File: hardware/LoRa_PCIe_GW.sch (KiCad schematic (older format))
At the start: 47 parts, among them U100 SX1303

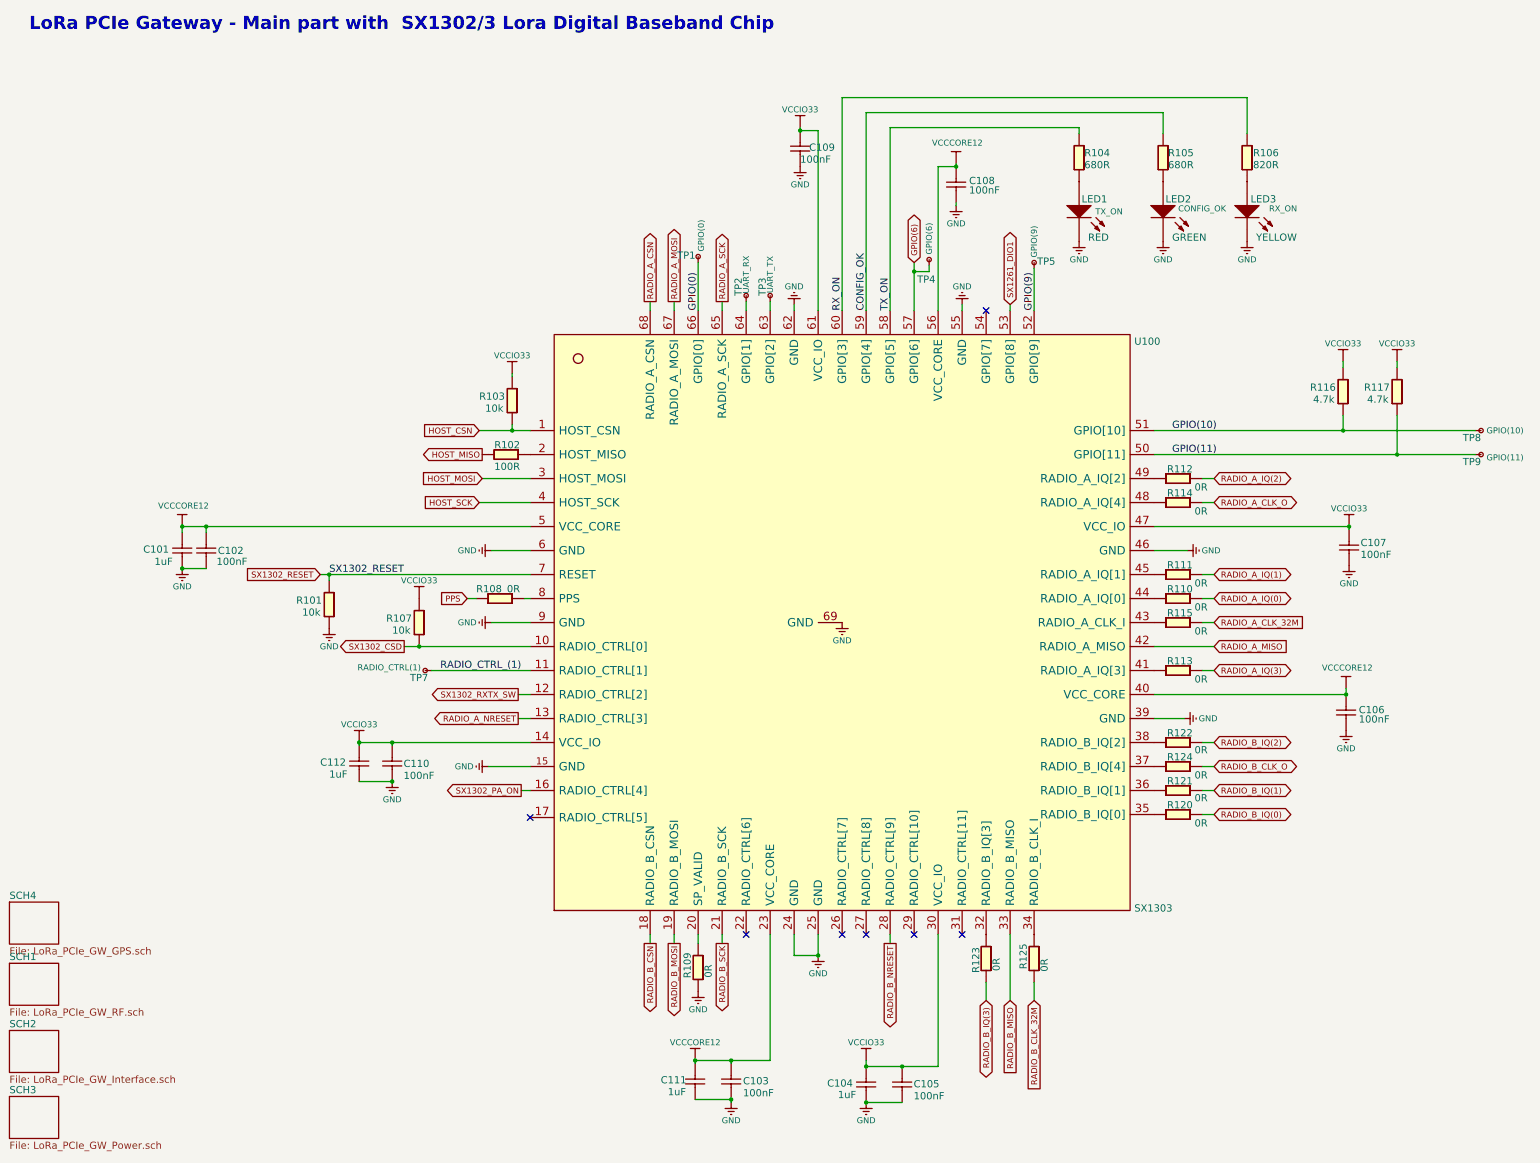
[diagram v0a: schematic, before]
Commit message: Updates according to Corecell_V3 Reference design.
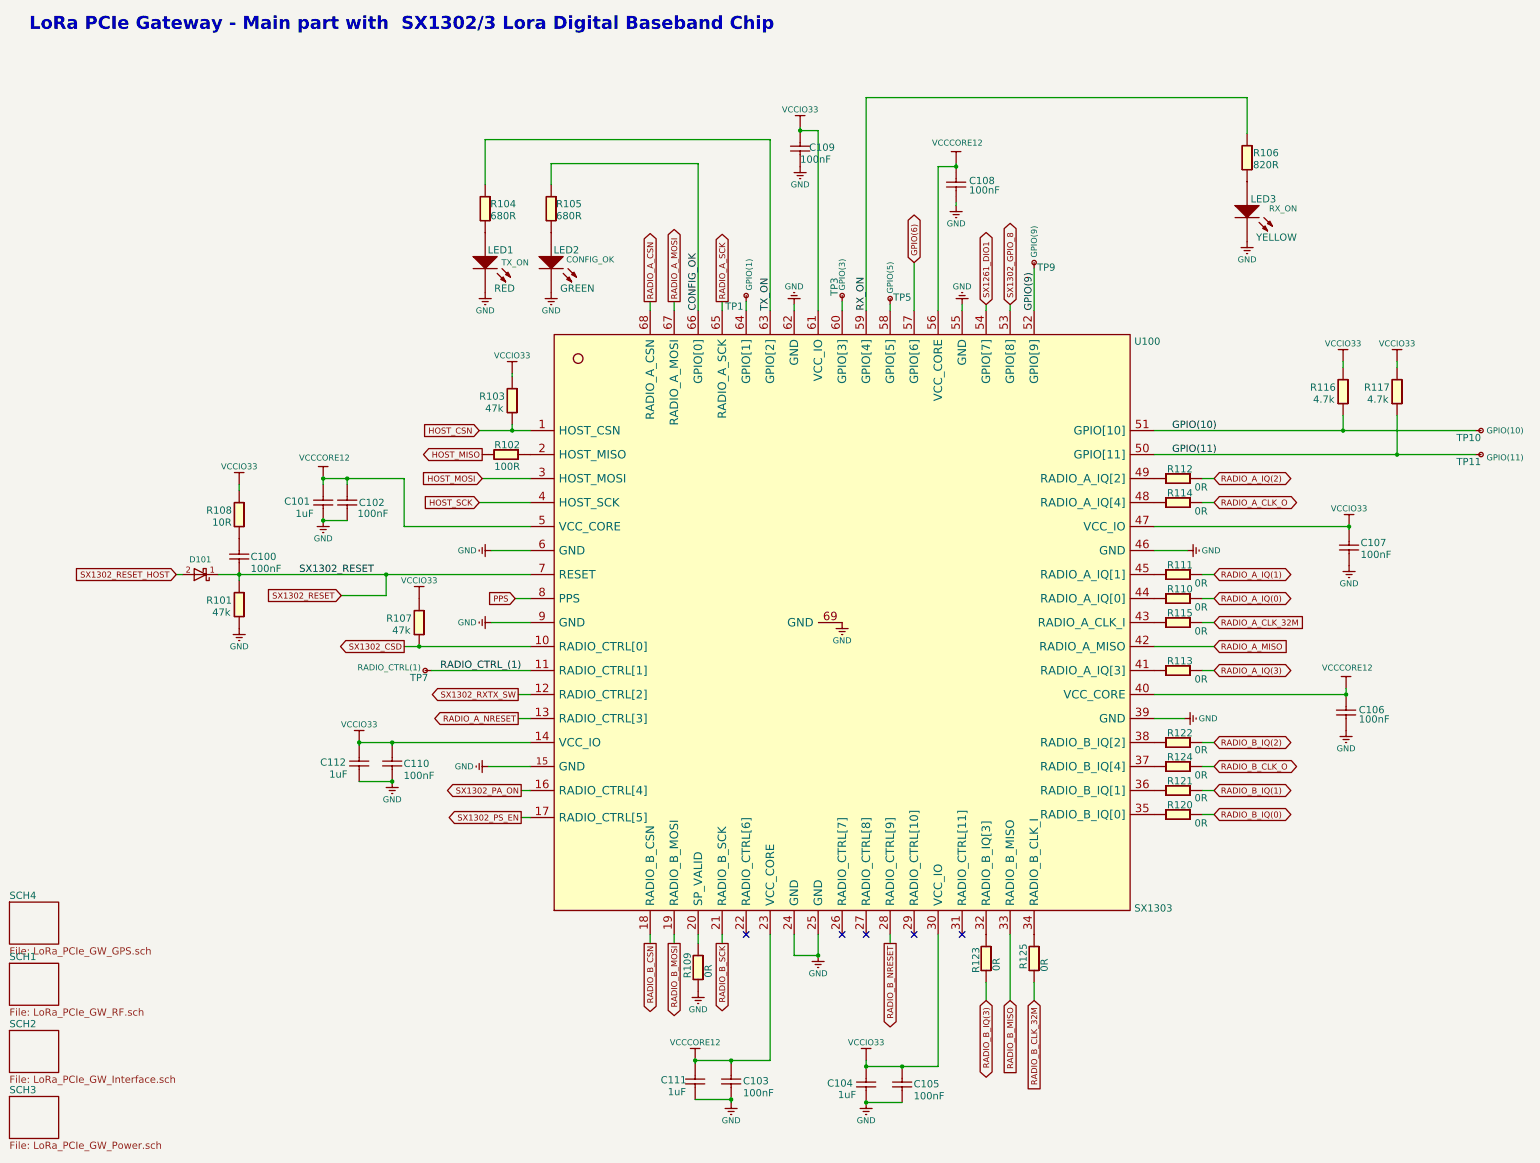
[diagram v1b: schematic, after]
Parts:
- removed TP2: NC, LoRa_PCIe_GW:PIN_SMD, symbol LoRa_PCIe_GW-rescue:test_pin-
- added C100: 100nF, LoRa_PCIe_GW:ccer_201_smd_small, symbol LoRa_PCIe_GW-rescue:Cap-
- added D101: BAT54, LoRa_PCIe_GW:SOD523, symbol LoRa_PCIe_GW-rescue:D_Schottky
- R101, R103, R107: value 10k -> 47k; Description 10 kOhms ±1% 0.05W, 1/20W Chip Resistor 0201 Thick Film -> 47 kOhms ±5% 0.05W, 1/20W Chip Resistor 0201 Thick Film; Part Number CRCW020110K0 -> CRCW020147K0; Price[1k] 0.037 -> 0.039; Supplier Link https://www.digikey.com/en/products/detail/vishay-dale/CRCW020110K0FKED/1967989 -> https://www.digikey.com/en/products/detail/vishay-dale/CRCW020147K0FKED/1968131
- R108: value 0R -> 10R; Description 0 Ohms Jumper 0.05W, 1/20W Chip Resistor 0201 (0603 Metric)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 -> 10 Ohms ±5% 0.05W, 1/20W Chip Resistor 0201 Thick Film; Part Number CRCW02010000Z0ED -> CRCW020110R0JNED; Price[1k] 0.006 -> 0.0052; Supplier Link https://www.digikey.com/en/products/detail/vishay-dale/CRCW02010000Z0ED/1178434?s=N4IgTCBcDaIMICU4HUAMZUEZU9QLVQFEAREAXQF8g -> https://www.digikey.com/en/products/detail/vishay-dale/CRCW020147K0FKED/1968131
- TP1: Label GPIO(0) -> GPIO(1)
- TP3: Label UART_TX -> GPIO(3)
- TP5: Label GPIO(9) -> GPIO(5)
- TP9: renamed from TP4; Label GPIO(6) -> GPIO(9)
- renumbered TP8 to TP10, TP9 to TP11
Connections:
- net CONFIG_OK: now also U100.66 (GPIO[0]); no longer U100.59 (GPIO[4])
- net GPIO(6): no longer TP9.1 (pin)
- net GPIO(9): now also TP9.1 (pin); no longer TP5.1 (pin)
- net PPS: now also U100.8 (PPS); no longer R108.1
- net RX_ON: now also U100.59 (GPIO[4]); no longer U100.60 (GPIO[3])
- net SX1261_DIO1: now also U100.54 (GPIO[7]); no longer U100.53 (GPIO[8])
- net SX1302_RESET: now also C100.1, D101.1
- net TX_ON: now also U100.63 (GPIO[2]); no longer U100.58 (GPIO[5])
- net VCCIO33: now also R108.2
- net SX1302_PS_EN: now reaches U100.17 (RADIO_CTRL[5])
- net at TP3.1 (pin): now also U100.60 (GPIO[3]); no longer U100.63 (GPIO[2])
- net at U100.64 (GPIO[1]): now also TP1.1 (pin)
- removed net GPIO(0): TP1.1 (pin), U100.66 (GPIO[0])
- new net: TP5.1 (pin), U100.58 (GPIO[5])
- new net: C100.2, R108.1
- new net SX1302_GPIO_8: U100.53 (GPIO[8])
- new net SX1302_RESET_HOST: D101.2
- no-connect marks 7 -> 5
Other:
- moved on the sheet: C101, C102, LED1, LED2, R101, R104, R105, TP1, TP3, TP5, TP9
